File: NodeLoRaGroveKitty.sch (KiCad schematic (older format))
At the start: 39 parts, among them P1 PICKIT PROGRAMMER, P2 Battery, P3 A0, P4 D9, P5 USB-Serial, P6 I2C, SW1 SW_BOOT, SW2 SW_RESET, U1 AP2112, U2 MCP73831T-2ATI/OT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

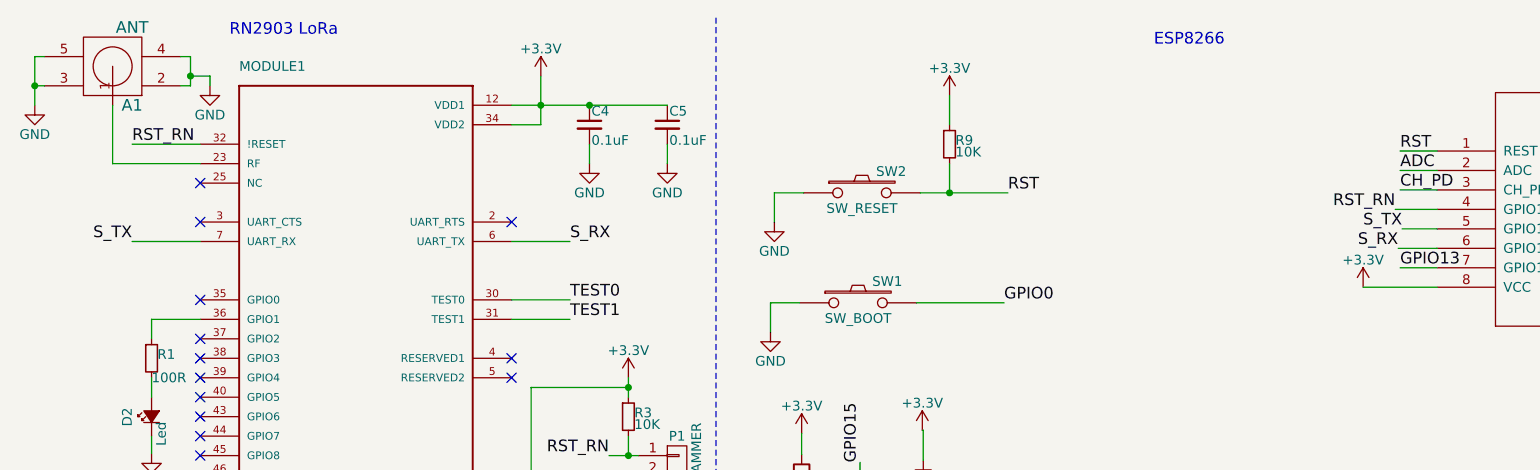
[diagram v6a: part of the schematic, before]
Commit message: Fix bug footprint
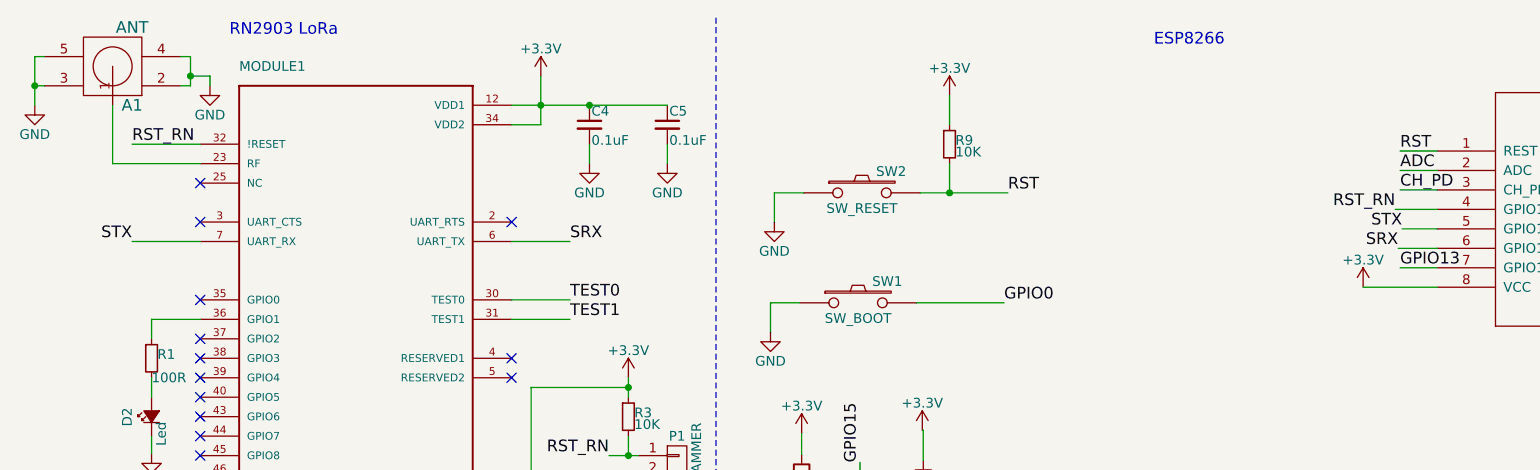
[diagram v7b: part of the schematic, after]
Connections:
- net S_RX renamed SRX
- net S_TX renamed STX
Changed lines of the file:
@@
 TEST1
 Text Label 3350 1650 0    60   ~ 0
-S_RX
+SRX
 Text Label 1100 1650 2    60   ~ 0
-S_TX
+STX
 Text Label 1100 1150 0    60   ~ 0
 RST_RN
@@
 RST_RN
 Text Label 7625 1585 2    60   ~ 0
-S_TX
+STX
 Text Label 7605 1685 2    60   ~ 0
-S_RX
+SRX
 Text Label 7615 1785 0    60   ~ 0
 GPIO13

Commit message: Update BOM
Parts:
- C1, C2, C6: manf# (none) -> GRM21BR61A106KE19L
- C3: manf# (none) -> GRM21BR71C105KA01L
- D1: manf# (none) -> NRVB120VLSFT1G
- D5: value 1N4001 -> 1N4001/S1BB; manf# (none) -> S1BB-13-F
- MODULE1: manf# (none) -> RN2903-I/RM095
- P5: footprint Pin_Headers:Pin_Header_Angled_1x06 -> Socket_Strips:Socket_Strip_Straight_1x06
- R1: value 100R -> 330R; manf# (none) -> ERJ-6GEYJ331V
- R10, R14, R8: manf# (none) -> AC0805KRX7R7BB104
- R12, R13: manf# (none) -> CPF0805B4K7E1
- R15, R3, R6, R7, R9: manf# (none) -> AF0805FR-0710KL
- R4, R5: manf# (none) -> ERJ-6GEYJ331V
- SW1, SW2: manf# (none) -> B3U-1000P
- U1: manf# (none) -> AP2112K-3.3TRG1
- U2: MP MCP73831T-2ATI/OT -> (none); Price 0.48 USD -> (none); manf# (none) -> MCP73831T-2DCI/OT
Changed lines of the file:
@@
 LIBS:RN2903-I_RM095
 LIBS:ESP32-footprints-Shem-Lib
+LIBS:Common-Parts-Library
 LIBS:NodeLoRaGroveKitty-cache
 EELAYER 25 0
@@
 F 7 "RN2483-I/RM095" H 2250 2150 50  0001 L CNN "MP"
 F 8 "Bad" H 2250 2150 50  0001 L CNN "Availability"
+F 9 "RN2903-I/RM095" H 2250 2150 60  0001 C CNN "manf#"
 	1    2250 2150
 	1    0    0    -1
@@
 F 2 "TO_SOT_Packages_SMD:SOT-23-5" H 2100 6300 60  0001 C CNN
 F 3 "" H 2100 6300 60  0000 C CNN
+F 4 "AP2112K-3.3TRG1" H 2100 6300 60  0001 C CNN "manf#"
 	1    2100 6300
 	1    0    0    -1
@@
 F 2 "Capacitors_SMD:C_0805_HandSoldering" H 1000 6250 50  0001 C CNN
 F 3 "" H 1000 6250 50  0000 C CNN
+F 4 "GRM21BR61A106KE19L" H 1000 6250 60  0001 C CNN "manf#"
 	1    1000 6250
 	1    0    0    -1
@@
 F 2 "Capacitors_SMD:C_0805_HandSoldering" H 2800 6250 50  0001 C CNN
 F 3 "" H 2800 6250 50  0000 C CNN
+F 4 "GRM21BR61A106KE19L" H 2800 6250 60  0001 C CNN "manf#"
 	1    2800 6250
 	1    0    0    -1
@@
 F 2 "Diodes_SMD:SOD-123" H 700 5850 50  0001 C CNN
 F 3 "" H 700 5850 50  0000 C CNN
+F 4 "NRVB120VLSFT1G" H 700 5850 60  0001 C CNN "manf#"
 	1    700  5850
 	0    -1   -1   0
@@
 F 2 "TO_SOT_Packages_SMD:SOT-23-5" H 4900 6400 50  0001 L CNN
 F 3 "SOT-23 Microchip" H 4050 6350 50  0001 L CNN
-F 4 "MCP73831T-2ATI/OT" H 4500 5550 50  0001 L CNN "MP"
+F 4 "MCP73831T-2DCI/OT" H 4500 5550 50  0001 L CNN "manf#"
 F 5 "Good" H 5550 6250 50  0001 L CNN "Availability"
 F 6 "MCP73831 Series Li-Ion/Li-Pol 15 mA - 500 mA 4.2 V Charge Controller - SOT-23-5" H 5350 5550 50  0001 L CNN "Description"
 F 7 "Microchip" H 4100 5550 50  0001 L CNN "MF"
-F 8 "0.48 USD" H 4350 6250 50  0001 L CNN "Price"
 	1    4950 6000
 	1    0    0    -1
@@
 F 2 "Resistors_SMD:R_0805_HandSoldering" H 4000 6200 50  0001 C CNN
 F 3 "" H 4000 6200 50  0000 C CNN
+F 4 "ERJ-6GEYJ331V" H 4000 6200 60  0001 C CNN "manf#"
 	1    4000 6200
 	0    1    1    0
@@
 F 2 "Resistors_SMD:R_0805_HandSoldering" H 4000 6500 50  0001 C CNN
 F 3 "" H 4000 6500 50  0000 C CNN
+F 4 "ERJ-6GEYJ331V" H 4000 6500 60  0001 C CNN "manf#"
 	1    4000 6500
 	0    1    1    0
@@
 F 2 "Capacitors_SMD:C_0805_HandSoldering" H 6250 6250 50  0001 C CNN
 F 3 "" H 6250 6250 50  0000 C CNN
+F 4 "GRM21BR61A106KE19L" H 6250 6250 60  0001 C CNN "manf#"
 	1    6250 6250
 	1    0    0    -1
@@
 F 2 "Resistors_SMD:R_0805_HandSoldering" H 8450 5600 50  0001 C CNN
 F 3 "" H 8450 5600 50  0000 C CNN
+F 4 "CPF0805B4K7E1" H 8450 5600 60  0001 C CNN "manf#"
 	1    8450 5600
 	1    0    0    -1
@@
 F 2 "Resistors_SMD:R_0805_HandSoldering" H 8200 5600 50  0001 C CNN
 F 3 "" H 8200 5600 50  0000 C CNN
+F 4 "CPF0805B4K7E1" H 8200 5600 60  0001 C CNN "manf#"
 	1    8200 5600
 	1    0    0    -1
@@
 F 2 "TIH:SW_B3U-1000P" H 4850 1400 50  0001 C CNN
 F 3 "" H 4850 1400 50  0000 C CNN
+F 4 "B3U-1000P" H 4850 1400 60  0001 C CNN "manf#"
 	1    4850 1400
 	1    0    0    -1
@@
 F 2 "Resistors_SMD:R_0805_HandSoldering" H 5300 1150 50  0001 C CNN
 F 3 "" H 5300 1150 50  0000 C CNN
+F 4 "AF0805FR-0710KL" H 5300 1150 60  0001 C CNN "manf#"
 	1    5300 1150
 	1    0    0    -1
@@
 F 2 "Resistors_SMD:R_0805_HandSoldering" H 3650 2550 50  0001 C CNN
 F 3 "" H 3650 2550 50  0000 C CNN
+F 4 "AF0805FR-0710KL" H 3650 2550 60  0001 C CNN "manf#"
 	1    3650 2550
 	1    0    0    -1
@@
 P 1200 2250
 F 0 "R1" H 1230 2270 50  0000 L CNN
-F 1 "100R" H 1200 2150 50  0000 L CNN
+F 1 "330R" H 1200 2150 50  0000 L CNN
 F 2 "Resistors_SMD:R_0805_HandSoldering" H 1200 2250 50  0001 C CNN
 F 3 "" H 1200 2250 50  0000 C CNN
+F 4 "ERJ-6GEYJ331V" H 1200 2250 60  0001 C CNN "manf#"
 	1    1200 2250
 	1    0    0    -1
@@
 F 2 "Capacitors_SMD:C_0805_HandSoldering" H 2950 6250 50  0001 C CNN
 F 3 "" H 2950 6250 50  0000 C CNN
+F 4 "GRM21BR71C105KA01L" H 2950 6250 60  0001 C CNN "manf#"
 	1    2950 6250
 	1    0    0    -1
@@
 F 2 "Resistors_SMD:R_0805_HandSoldering" V 4470 2895 50  0001 C CNN
 F 3 "" H 4540 2895 50  0000 C CNN
+F 4 "AF0805FR-0710KL" V 4540 2895 60  0001 C CNN "manf#"
 	1    4540 2895
 	1    0    0    -1
@@
 F 2 "Resistors_SMD:R_0805_HandSoldering" V 4770 3045 50  0001 C CNN
 F 3 "" H 4840 3045 50  0000 C CNN
+F 4 "AF0805FR-0710KL" V 4840 3045 60  0001 C CNN "manf#"
 	1    4840 3045
 	1    0    0    -1
@@
 F 2 "Resistors_SMD:R_0805_HandSoldering" V 4830 3870 50  0001 C CNN
 F 3 "" H 4900 3870 50  0000 C CNN
+F 4 "AC0805KRX7R7BB104" V 4900 3870 60  0001 C CNN "manf#"
 	1    4900 3870
 	0    1    1    0
@@
 F 2 "Resistors_SMD:R_0805_HandSoldering" V 5250 3870 50  0001 C CNN
 F 3 "" H 5320 3870 50  0000 C CNN
+F 4 "AC0805KRX7R7BB104" V 5320 3870 60  0001 C CNN "manf#"
 	1    5320 3870
 	0    1    1    0
@@
 F 0 "P5" H 10055 3845 50  0000 C CNN
 F 1 "USB-Serial" V 10155 3495 50  0000 C CNN
-F 2 "Pin_Headers:Pin_Header_Angled_1x06" H 10055 3495 50  0001 C CNN
+F 2 "Socket_Strips:Socket_Strip_Straight_1x06" H 10055 3495 50  0001 C CNN
 F 3 "" H 10055 3495 50  0000 C CNN
 	1    10055 3495
@@
 F 2 "TIH:SW_B3U-1000P" H 4830 1965 50  0001 C CNN
 F 3 "" H 4830 1965 50  0000 C CNN
+F 4 "B3U-1000P" H 4830 1965 60  0001 C CNN "manf#"
 	1    4830 1965
 	1    0    0    -1
@@
 P 8065 3670
 F 0 "D5" H 8065 3770 50  0000 C CNN
-F 1 "1N4001" H 8065 3570 50  0000 C CNN
+F 1 "1N4001/S1BB" H 8065 3570 50  0000 C CNN
 F 2 "Diodes_SMD:SMB_Handsoldering" H 8065 3670 50  0001 C CNN
 F 3 "" H 8065 3670 50  0000 C CNN
+F 4 "S1BB-13-F" H 8065 3670 60  0001 C CNN "manf#"
 	1    8065 3670
 	1    0    0    -1
@@
 F 2 "Resistors_SMD:R_0805_HandSoldering" V 5810 3870 50  0001 C CNN
 F 3 "" H 5880 3870 50  0000 C CNN
+F 4 "AC0805KRX7R7BB104" V 5880 3870 60  0001 C CNN "manf#"
 	1    5880 3870
 	0    1    1    0
@@
 F 2 "Resistors_SMD:R_0805_HandSoldering" V 5095 2925 50  0001 C CNN
 F 3 "" H 5165 2925 50  0000 C CNN
+F 4 "AF0805FR-0710KL" V 5165 2925 60  0001 C CNN "manf#"
 	1    5165 2925
 	1    0    0    -1
